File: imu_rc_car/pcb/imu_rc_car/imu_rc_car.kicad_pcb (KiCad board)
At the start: 2 copper layers, 100 x 82.3 mm, 35 parts, among them J1 LiPo Battery, J2 Left Terminal, J3 Right Terminal, J4 Prox Sensor FS, J5 Prox Sensor LS, J6 Prox Sensor RS, J7 Prox Sensor BS, J8 Encoder F, J9 Encoder B, Q1 IRLML6344TRPBF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

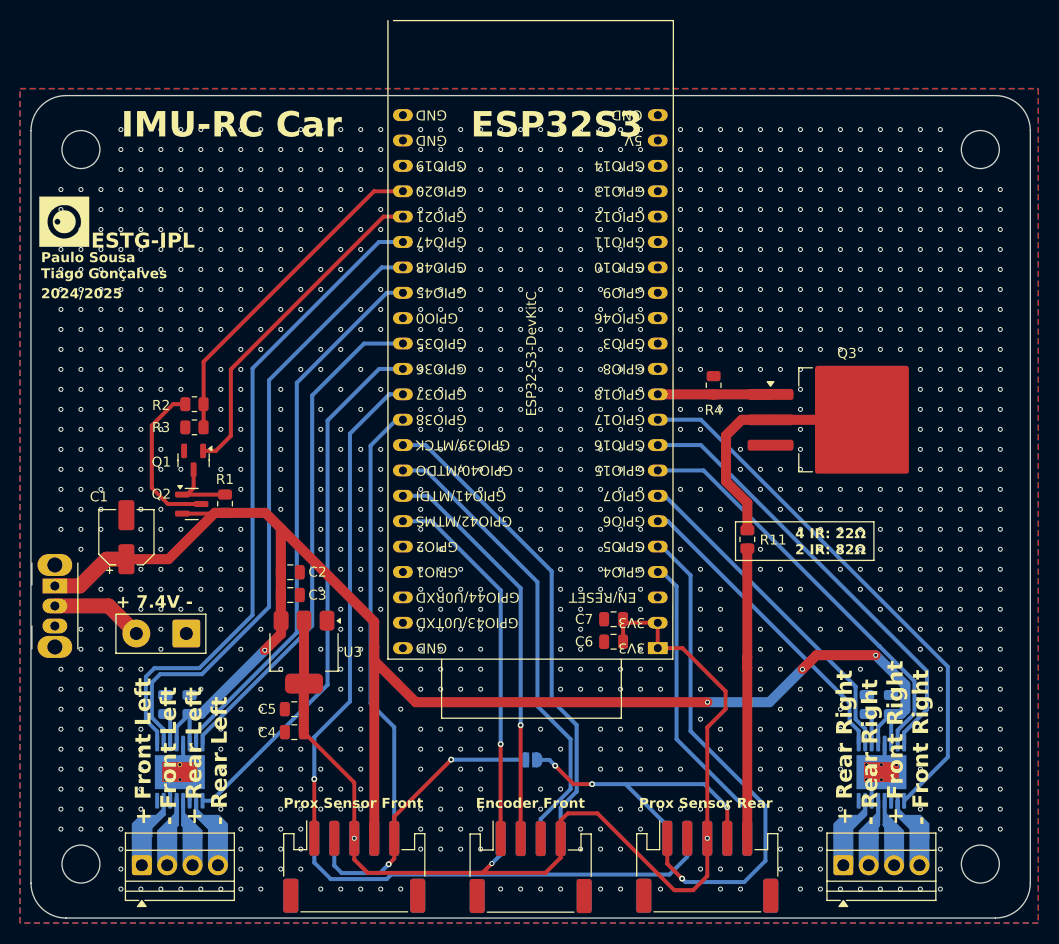
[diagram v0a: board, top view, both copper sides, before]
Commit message: commit #35
fixed error in pcb for DRV8833
added 4 motor support for code
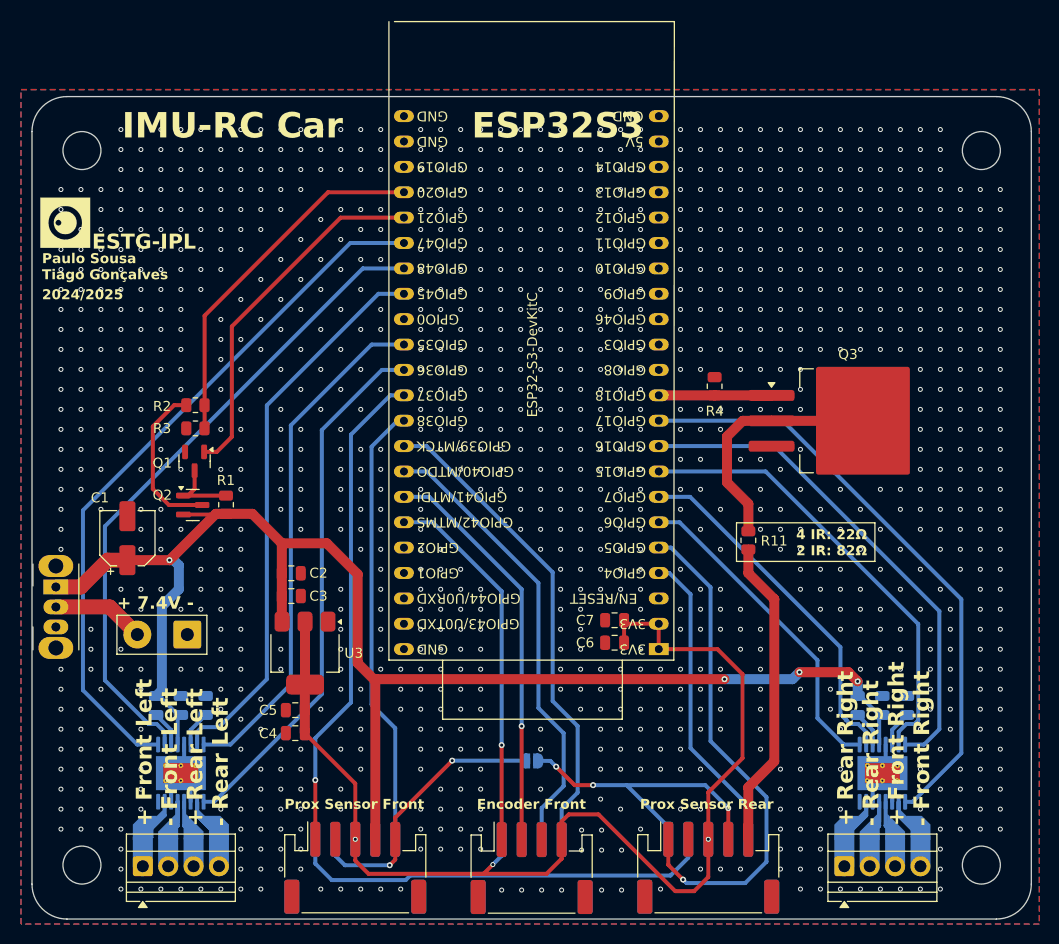
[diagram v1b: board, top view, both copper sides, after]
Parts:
- added C12: 2u2F, Capacitor_SMD:C_0805_2012Metric, B.Cu at (182.7, 115.6)
- added C13: 10uF, Capacitor_SMD:C_0805_2012Metric, B.Cu at (180.2, 115.6)
- C10: value 2.2uF -> 10uF
- C8: value 2.2uF -> 10nF
- C9: value 10nF -> 2u2F
- moved C10 71.1 mm to (110.0, 115.6)
- moved C9 4.03 mm to (112.5, 115.6), turned to -90 degrees
- moved C8 3.35 mm to (107.5, 115.6), turned to -90 degrees
- moved C11 0.93 mm to (177.7, 115.6), turned to -90 degrees
- moved C4 0.14 mm to (121.5, 118.4)
- moved R1 0.14 mm to (114.5, 95.5)
- moved C1 0.14 mm to (104.7, 98.9)
- moved C2 0.14 mm to (121.0, 102.4)
- moved C3 0.14 mm to (121.0, 104.7)
- moved C5 0.14 mm to (121.5, 116.1)
- moved G*** 0.14 mm to (98.4, 67.3)
- moved J1 0.14 mm to (110.6, 108.5)
- moved J4 0.14 mm to (127.5, 131.9)
- moved J5 0.14 mm to (127.5, 131.9)
- moved Q1 0.14 mm to (111.4, 91.2)
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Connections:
- C11 pad 1: Net-(U6-VCP) -> +7V4
- C11 pad 2: GND -> Net-(U6-VCP)
- C8 pad 2: GND -> Net-(U7-VCP)
- C9 pad 1: Net-(U7-VCP) -> GND
- C9 pad 2: GND -> Net-(U7-VINT)
- U6 pad 14: +7V4 -> Net-(U6-VINT)
- U7 pad 14: +7V4 -> Net-(U7-VINT)
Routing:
- net +7V4: track 165.0 -> 153.2 mm
- net AIN3: track 44.5 -> 50.8 mm
- net STBYB: track 54.5 -> 60.7 mm
- net BIN1: track 65.3 -> 71.0 mm
- net AIN4: track 41.4 -> 45.6 mm
- net Net-(U7-VINT): track 0.00 -> 3.58 mm
- net Net-(U6-VINT): track 0.00 -> 3.58 mm
- net +3V3: track 111.9 -> 115.2 mm
- net BIN2: track 62.2 -> 65.4 mm
- net BATT_READ: track 33.6 -> 36.3 mm
- net BATT_READ_EN: track 33.6 -> 36.2 mm
- net SO: track 29.0 -> 31.2 mm
- net BIN4: track 34.1 -> 36.0 mm
- net AIN2: track 54.6 -> 56.2 mm
- net BIN3: track 31.2 -> 32.7 mm
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
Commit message: commit #38
imu rc car v1.1.1:
Added ON/OFF text for switch
Fixed no ADC GPIOs for 2 prox sensors
Fixed battery reading
Bigger text in Prox Sensors and Encoders
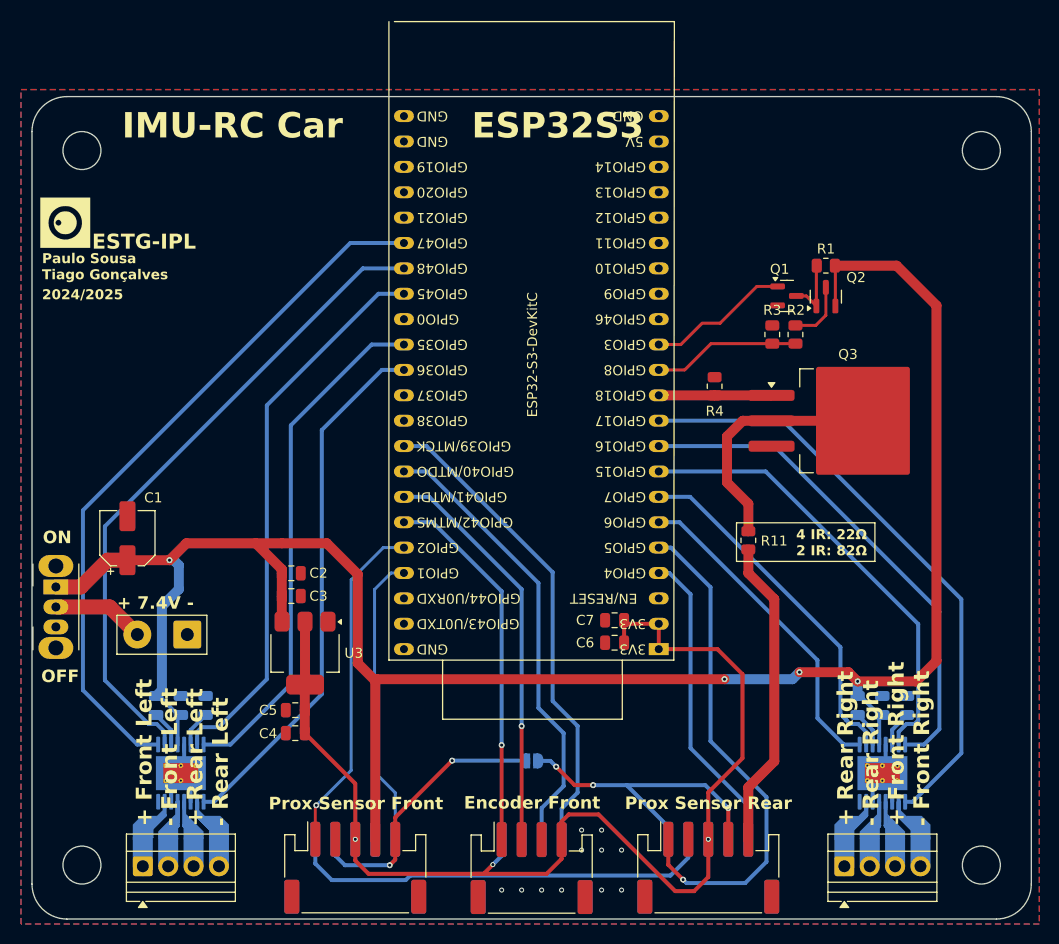
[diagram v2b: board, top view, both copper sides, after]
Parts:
- moved Q2 66.7 mm to (174.5, 74.7), turned to 90 degrees
- moved R1 64.6 mm to (174.5, 71.6), turned to 0 degrees
- moved Q1 61.5 mm to (170.6, 74.6), turned to 0 degrees
- moved R2 60.5 mm to (171.5, 78.5), turned to -90 degrees
- moved R3 58.5 mm to (169.2, 78.5), turned to 90 degrees
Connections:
- U1 pad 12: unconnected-(U1-GPIO8/ADC1_CH7-Pad12) -> BATT_READ
- U1 pad 13: unconnected-(U1-GPIO3/ADC1_CH2-Pad13) -> BATT_READ_EN
- U1 pad 26: BATT_READ -> unconnected-(U1-GPIO20/USB_D+-Pad26)
- U1 pad 27: BATT_READ_EN -> unconnected-(U1-GPIO21-Pad27)
- U1 pad 34: PRX_FS -> unconnected-(U1-GPIO37-Pad34)
- U1 pad 35: PRX_LS -> unconnected-(U1-GPIO38-Pad35)
- U1 pad 40: unconnected-(U1-GPIO2/ADC1_CH1-Pad40) -> PRX_FS
- U1 pad 41: unconnected-(U1-GPIO1/ADC1_CH0-Pad41) -> PRX_LS
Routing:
- net +7V4: track 153.2 -> 207.7 mm
- net BATT_READ_EN: track 36.2 -> 14.3 mm
- net BATT_READ: track 36.3 -> 14.8 mm
- net PRX_LS: track 44.9 -> 29.5 mm
- net PRX_FS: track 49.0 -> 34.1 mm
- net Net-(Q2-D): track 16.1 -> 6.26 mm
- net Net-(Q1-D): track 7.50 -> 6.47 mm
- net GND: vias 1220 -> 11
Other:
- board text added: "- 7.4V +"
- board text added: "OFF"
- board text added: "ON"
- board text added: "v1.1.1"
- board text removed: "v1.1.0"
